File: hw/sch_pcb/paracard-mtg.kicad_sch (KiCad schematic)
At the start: 7 parts

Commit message: Update schematics. Preparation to resolve #2.
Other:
- company: ORBISYS www.orbisys.sk -> MLAB.cz
- title: MPPB01A -> MPPB01B
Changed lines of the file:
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@@
   (paper "B")
   (title_block
-    (title "MPPB01A")
-    (date "09 May 2014")
-    (rev "REV 0.1")
-    (company "ORBISYS www.orbisys.sk")
+    (title "MPPB01B")
+    (date "2022-03-24")
+    (company "MLAB.cz")
     (comment 1 "VERSION 1")
     (comment 2 "Paralella reduction board")
-    (comment 3 "Maksim Rezenov, Jakub kakona")
+    (comment 3 "Maksim Rezenov, Jakub Kakona")
   )
   (junction (at 223.52 124.46) (diameter 0) (color 0 0 0 0)

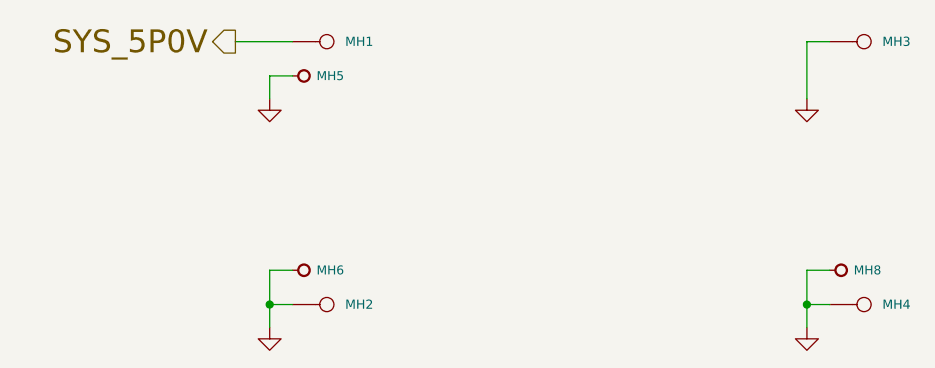
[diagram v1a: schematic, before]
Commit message: Adding pull-up resistor to resolve #1.
Geometric preparation for #2.
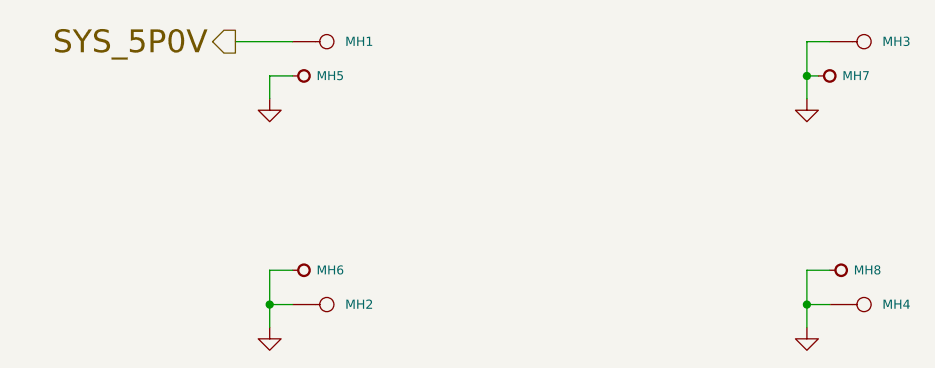
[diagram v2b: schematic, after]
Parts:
- added MH7: HOLE, Mlab_Mechanical:MountingHole_3mm, symbol MLAB_MECHANICAL:HOLE
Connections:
- net GND: now also MH7.1
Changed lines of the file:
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@@
   (junction (at 223.52 124.46) (diameter 0) (color 0 0 0 0)
   )
+  (junction (at 223.52 99.06) (diameter 0) (color 0 0 0 0)
+  )
   (junction (at 163.83 124.46) (diameter 0) (color 0 0 0 0)
   )
+  (wire (pts (xy 223.52 99.06) (xy 223.52 101.6))
+    (stroke (width 0) (type default) (color 0 0 0 0))
+  )
   (wire (pts (xy 226.06 120.65) (xy 223.52 120.65))
     (stroke (width 0) (type default) (color 0 0 0 0))
@@
     (stroke (width 0) (type default) (color 0 0 0 0))
   )
+  (wire (pts (xy 223.52 99.06) (xy 224.79 99.06))
+    (stroke (width 0) (type default) (color 0 0 0 0))
+  )
   (wire (pts (xy 160.02 95.25) (xy 166.37 95.25))
     (stroke (width 0) (type default) (color 0 0 0 0))
   )
-  (wire (pts (xy 223.52 95.25) (xy 223.52 101.6))
+  (wire (pts (xy 223.52 95.25) (xy 223.52 99.06))
     (stroke (width 0) (type default) (color 0 0 0 0))
   )
@@
       (effects (font (size 1.524 1.524)))
     )
+    (pin "1")
+  )
+  (symbol (lib_id "MLAB_MECHANICAL:HOLE") (at 226.06 99.06 180) (unit 1)
+    (in_bom yes) (on_board yes)
+    (property "Reference" "MH7" (id 0) (at 227.457 99.06 0)
+      (effects (font (size 0.9906 0.9906)) (justify right))
+    )
+    (property "Value" "HOLE" (id 1) (at 225.6028 101.7778 0)
+      (effects (font (size 1.524 1.524)) hide)
+    )
+    (property "Footprint" "Mlab_Mechanical:MountingHole_3mm" (id 2) (at 227.457 100.0252 0)
+      (effects (font (size 1.524 1.524)) (justify right) hide)
+    )
+    (property "Datasheet" "" (id 3) (at 226.06 99.06 0)
+      (effects (font (size 1.524 1.524)))
+    )

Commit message: Priprava pro osazeni
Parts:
- MH1, MH2, MH3, MH4: value MTG\PTH\125\SQ -> (none); footprint MTG_PTH_125_SQ -> (none)
- MH5, MH6, MH7, MH8: value HOLE -> (none); footprint Mlab_Mechanical:MountingHole_3mm -> (none)
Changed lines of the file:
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@@
       (effects (font (size 1.016 1.016)) (justify left))
     )
-    (property "Value" "MTG\\PTH\\125\\SQ" (id 1) (at 170.18 93.853 0)
+    (property "Value" "" (id 1) (at 170.18 93.853 0)
       (effects (font (size 0.762 0.762)) hide)
     )
-    (property "Footprint" "MTG_PTH_125_SQ" (id 2) (at 169.672 97.79 0)
+    (property "Footprint" "" (id 2) (at 169.672 97.79 0)
       (effects (font (size 1.27 1.27)) hide)
     )
@@
       (effects (font (size 1.016 1.016)) (justify left))
     )
-    (property "Value" "MTG\\PTH\\125\\SQ" (id 1) (at 229.87 93.853 0)
+    (property "Value" "" (id 1) (at 229.87 93.853 0)
       (effects (font (size 0.762 0.762)) hide)
     )
-    (property "Footprint" "MTG_PTH_125_SQ" (id 2) (at 229.362 97.79 0)
+    (property "Footprint" "" (id 2) (at 229.362 97.79 0)
       (effects (font (size 1.27 1.27)) hide)
     )
@@
       (effects (font (size 1.016 1.016)) (justify left))
     )
-    (property "Value" "MTG\\PTH\\125\\SQ" (id 1) (at 170.18 123.063 0)
+    (property "Value" "" (id 1) (at 170.18 123.063 0)
       (effects (font (size 0.762 0.762)) hide)
     )
-    (property "Footprint" "MTG_PTH_125_SQ" (id 2) (at 169.672 127 0)
+    (property "Footprint" "" (id 2) (at 169.672 127 0)
       (effects (font (size 1.27 1.27)) hide)
     )
@@
       (effects (font (size 1.016 1.016)) (justify left))
     )
-    (property "Value" "MTG\\PTH\\125\\SQ" (id 1) (at 229.87 123.063 0)
+    (property "Value" "" (id 1) (at 229.87 123.063 0)
       (effects (font (size 0.762 0.762)) hide)
     )
-    (property "Footprint" "MTG_PTH_125_SQ" (id 2) (at 229.362 127 0)
+    (property "Footprint" "" (id 2) (at 229.362 127 0)
       (effects (font (size 1.27 1.27)) hide)
     )
@@
       (effects (font (size 0.9906 0.9906)) (justify right))
     )
-    (property "Value" "HOLE" (id 1) (at 167.1828 101.8032 0)
+    (property "Value" "" (id 1) (at 167.1828 101.8032 0)
       (effects (font (size 1.524 1.524)) hide)
     )
-    (property "Footprint" "Mlab_Mechanical:MountingHole_3mm" (id 2) (at 169.037 100.0252 0)
+    (property "Footprint" "" (id 2) (at 169.037 100.0252 0)
       (effects (font (size 1.524 1.524)) (justify right) hide)
     )
@@
       (effects (font (size 0.9906 0.9906)) (justify right))
     )
-    (property "Value" "HOLE" (id 1) (at 226.8728 123.3678 0)
+    (property "Value" "" (id 1) (at 226.8728 123.3678 0)
       (effects (font (size 1.524 1.524)) hide)
     )
-    (property "Footprint" "Mlab_Mechanical:MountingHole_3mm" (id 2) (at 228.727 121.6152 0)
+    (property "Footprint" "" (id 2) (at 228.727 121.6152 0)
       (effects (font (size 1.524 1.524)) (justify right) hide)
     )
@@
       (effects (font (size 0.9906 0.9906)) (justify right))
     )
-    (property "Value" "HOLE" (id 1) (at 167.1828 123.3678 0)
+    (property "Value" "" (id 1) (at 167.1828 123.3678 0)
       (effects (font (size 1.524 1.524)) hide)
     )
-    (property "Footprint" "Mlab_Mechanical:MountingHole_3mm" (id 2) (at 169.037 121.6152 0)
+    (property "Footprint" "" (id 2) (at 169.037 121.6152 0)
       (effects (font (size 1.524 1.524)) (justify right) hide)
     )
@@
       (effects (font (size 0.9906 0.9906)) (justify right))
     )
-    (property "Value" "HOLE" (id 1) (at 225.6028 101.7778 0)
+    (property "Value" "" (id 1) (at 225.6028 101.7778 0)
       (effects (font (size 1.524 1.524)) hide)
     )
-    (property "Footprint" "Mlab_Mechanical:MountingHole_3mm" (id 2) (at 227.457 100.0252 0)
+    (property "Footprint" "" (id 2) (at 227.457 100.0252 0)
       (effects (font (size 1.524 1.524)) (justify right) hide)
     )

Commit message: update assets, save as 7
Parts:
- MH1, MH2, MH3, MH4: value (none) -> MTG\PTH\125\SQ; footprint (none) -> MTG_PTH_125_SQ
- MH5, MH6, MH7, MH8: value (none) -> HOLE; footprint (none) -> Mlab_Mechanical:MountingHole_3mm
